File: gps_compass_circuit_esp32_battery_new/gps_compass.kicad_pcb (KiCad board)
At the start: 2 copper layers, 80 x 46 mm, 58 parts, among them J1 USB_C_Receptacle_PowerOnly_6P, Q1 MMBTA92, U1 MCP1700x-330xxTT, U3 LTC4054ES5-4.2

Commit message: Aggiornamenti vari
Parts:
- moved R4 11.3 mm to (77.2, 69.8), turned to 180 degrees
- moved C3 0.97 mm to (76.5, 77.6)
- moved C4 0.97 mm to (78.1, 77.6)
- moved C8 0.97 mm to (76.5, 74.1)
- moved C9 0.97 mm to (78.1, 74.1)
- moved GPS1 0.95 mm to (87.5, 76.9)
- moved Q1 0.41 mm to (76.0, 78.4)
- moved En 0.10 mm to (117.1, 81.8)
- moved Prog 0.10 mm to (117.1, 77.8)
- renumbered En1 to En, Prog1 to Prog
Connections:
- microsd1 pad 11: (no net) -> GND
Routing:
- net Net-(GPS1-~{RESET}): track 2.39 -> 11.3 mm
- net GND: track 3.26 -> 5.71 mm, vias 9 -> 11
- net VCC: track 151.6 -> 153.0 mm
- net SDA: track 80.6 -> 79.7 mm
- net Net-(GPS1-TXD): track 12.3 -> 11.5 mm
- net Net-(GPS1-RXD): track 9.29 -> 8.63 mm
- net Net-(ESP32-S1-EN): track 51.0 -> 51.6 mm
- net +3V3: track 78.3 -> 77.7 mm
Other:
- outline, holes or cut-outs redrawn
- board text added: "Walk, lost yourself, return"

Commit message: migliorati posizionamenti gnd
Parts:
- moved C1 2.11 mm to (82.5, 68.2)
- moved BT1 2.02 mm to (77.8, 63.0)
- moved C17 1.18 mm to (119.5, 49.6)
- moved C18 1.18 mm to (119.5, 47.9)
- moved R5 0.70 mm to (119.5, 51.3)
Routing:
- net Net-(BT1-+): track 25.8 -> 28.7 mm
- net Net-(ESP32-S1-EN): track 51.6 -> 51.0 mm
- net VCC: track 153.0 -> 152.5 mm
- net GND: vias 11 -> 13
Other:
- board text added: "Dade3e 2023 Esp32 GpsCompass"

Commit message: Aggiornamenti vari
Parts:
- J1: moved to F.Cu
- moved R8 7.21 mm to (71.8, 59.5), turned to 90 degrees
- moved J1 5.95 mm to (69.3, 60.0), turned to -90 degrees
- moved C19 3.35 mm to (128.3, 54.4)
- moved C16 3.35 mm to (131.8, 54.4)
- moved C3 2.65 mm to (77.3, 75.1), turned to 180 degrees
- moved C1 2.47 mm to (82.8, 70.7)
- moved C8 2.36 mm to (77.3, 71.9), turned to 180 degrees
- moved C2 2.04 mm to (70.3, 74.4)
- moved D1 1.90 mm to (72.3, 68.9), turned to 90 degrees
- moved C4 1.23 mm to (77.3, 76.7), turned to 180 degrees
- moved C9 1.02 mm to (77.3, 73.5), turned to 180 degrees
- moved R7 0.76 mm to (66.4, 70.5)
- moved C10 0.50 mm to (113.9, 81.2)
- moved C11 0.50 mm to (112.2, 81.2)
- moved R16 0.50 mm to (93.7, 52.4)
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- renumbered ESP1 to ESP, ESP32-S1 to ESP32-S, GPS1 to GPS, LCD1 to LCD, LED1 to LED, MAIN1 to MAIN, Oled1 to Oled, Serial1 to Serial, microsd1 to microsd
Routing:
- net VCC: track 152.5 -> 122.6 mm, vias 0 -> 1
- net SDA: track 79.7 -> 61.9 mm, vias 1 -> 2
- net SCL: track 74.0 -> 63.3 mm
- net Net-(BT1-+): track 28.7 -> 36.7 mm
- net MISO: track 52.9 -> 46.6 mm, vias 0 -> 2
- net Net-(J1-CC2): track 11.5 -> 6.11 mm
- net +3V3: track 77.7 -> 73.4 mm
- net Net-(Serial1-Pin_3): track 28.8 -> 25.5 mm
- net Net-(ESP32-S1-IO0): track 23.1 -> 26.3 mm
- net battery_level: track 41.1 -> 38.2 mm
- net GND: track 5.71 -> 3.26 mm, vias 13 -> 19
- net Net-(D1-K): track 49.6 -> 47.3 mm
- net Net-(ESP32-S1-EN): track 51.0 -> 52.8 mm
- net B1: track 17.8 -> 19.2 mm
- net lcd_cs: track 22.4 -> 23.7 mm
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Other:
- outline, holes or cut-outs redrawn
- board text added: "GND"
- board text added: "RX"
- board text added: "TX"
- board text added: "off on"

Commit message: Aggiunto led rgb seriale
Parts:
- removed LED: LED, LED_THT:LED_D3.0mm
- removed R6: R, Resistor_SMD:R_0603_1608Metric_Pad0.98x0.95mm_HandSolder
- added C12: 0,1uF, Capacitor_SMD:C_0603_1608Metric_Pad1.08x0.95mm_HandSolder, F.Cu at (72.4, 58.2)
- added C13: 1uF, Capacitor_SMD:C_0603_1608Metric_Pad1.08x0.95mm_HandSolder, F.Cu at (72.4, 56.5)
- added D3: WS2812B, LED_SMD:LED_WS2812B_PLCC4_5.0x5.0mm_P3.2mm, F.Cu at (72.5, 52.0)
- moved Serial1 0.36 mm to (67.9, 55.7)
- renumbered ESP to ESP1, ESP32-S to ESP32-S1, En to En1, GPS to GPS1, LCD to LCD1, MAIN to MAIN1, Oled to Oled1, Prog to Prog1, Serial to Serial1, microsd to microsd1
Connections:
- microsd1 pad 11: GND -> (no net)
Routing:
- net VCC: track 122.6 -> 144.4 mm
- net Net-(LED1-K): track 3.19 -> 0.00 mm
- net Net-(D3-DIN): track 47.1 -> 49.0 mm
- net Net-(Serial1-Pin_2): track 25.9 -> 25.1 mm

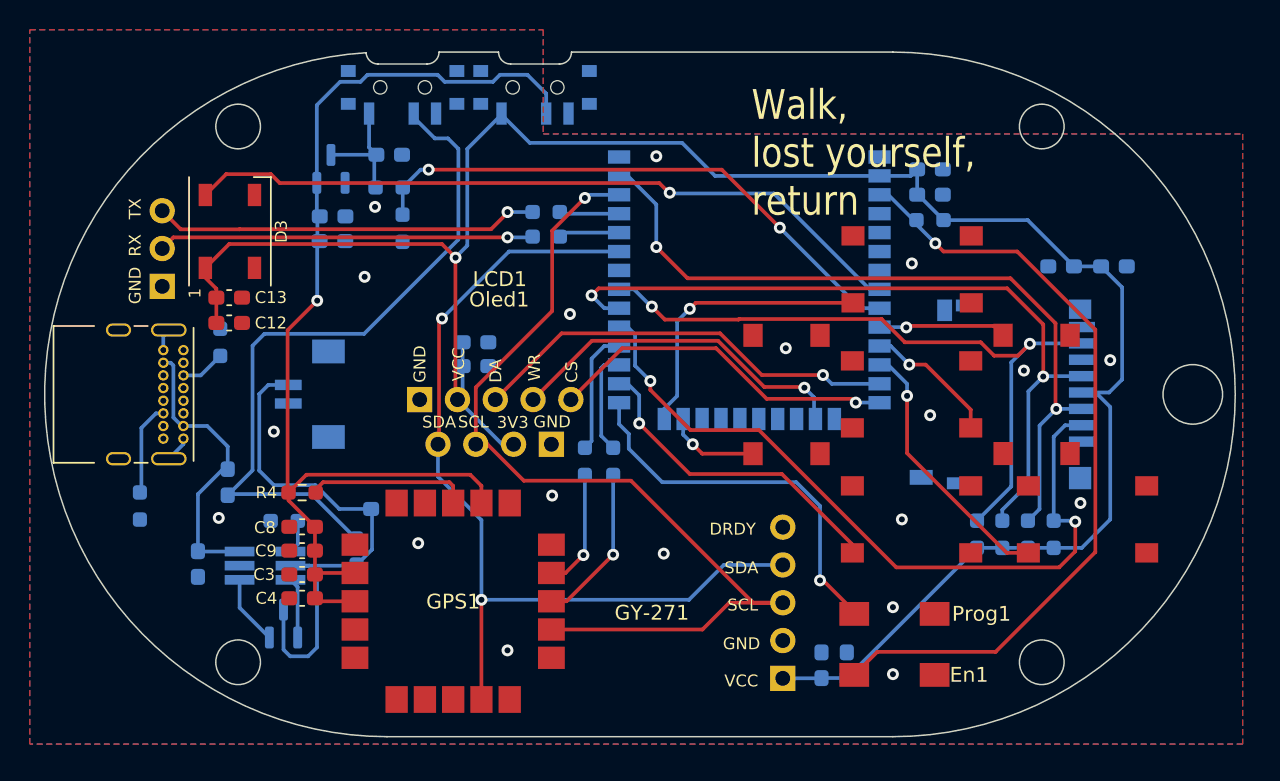
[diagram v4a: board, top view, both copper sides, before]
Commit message: Riprestinato led non rgb
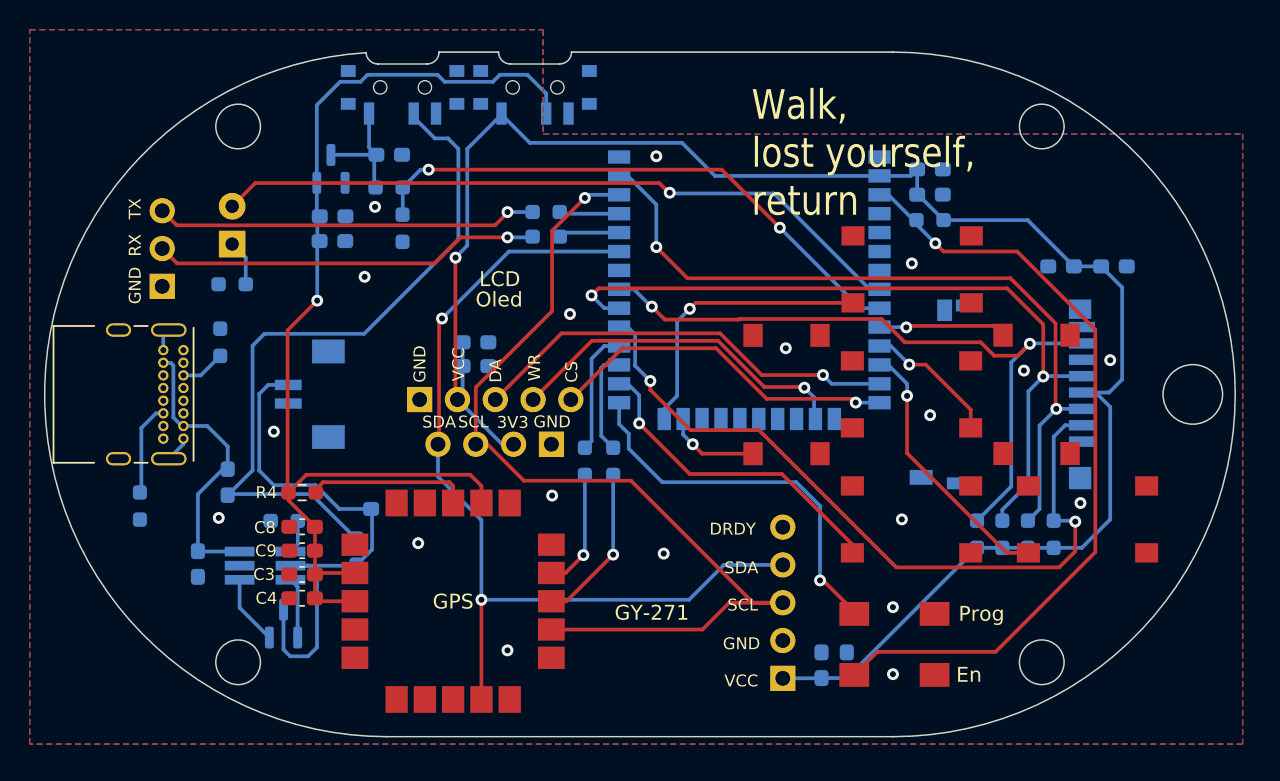
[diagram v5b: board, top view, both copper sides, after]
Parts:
- removed C12: 0,1uF, Capacitor_SMD:C_0603_1608Metric_Pad1.08x0.95mm_HandSolder
- removed C13: 1uF, Capacitor_SMD:C_0603_1608Metric_Pad1.08x0.95mm_HandSolder
- removed D3: WS2812B, LED_SMD:LED_WS2812B_PLCC4_5.0x5.0mm_P3.2mm
- added LED: LED, LED_THT:LED_D3.0mm, B.Cu at (72.6, 52.9)
- added R6: R, Resistor_SMD:R_0603_1608Metric_Pad0.98x0.95mm_HandSolder, B.Cu at (72.6, 55.6)
- renumbered ESP1 to ESP, ESP32-S1 to ESP32-S, En1 to En, GPS1 to GPS, LCD1 to LCD, MAIN1 to MAIN, Oled1 to Oled, Prog1 to Prog, Serial1 to Serial, microsd1 to microsd
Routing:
- net VCC: track 144.4 -> 122.6 mm
- net Net-(D3-K): track 0.00 -> 3.08 mm
- net Net-(D3-A): track 49.0 -> 47.0 mm
- net Net-(Serial1-Pin_2): track 25.1 -> 26.0 mm
